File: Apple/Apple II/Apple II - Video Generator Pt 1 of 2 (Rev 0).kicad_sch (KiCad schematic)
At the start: 19 parts

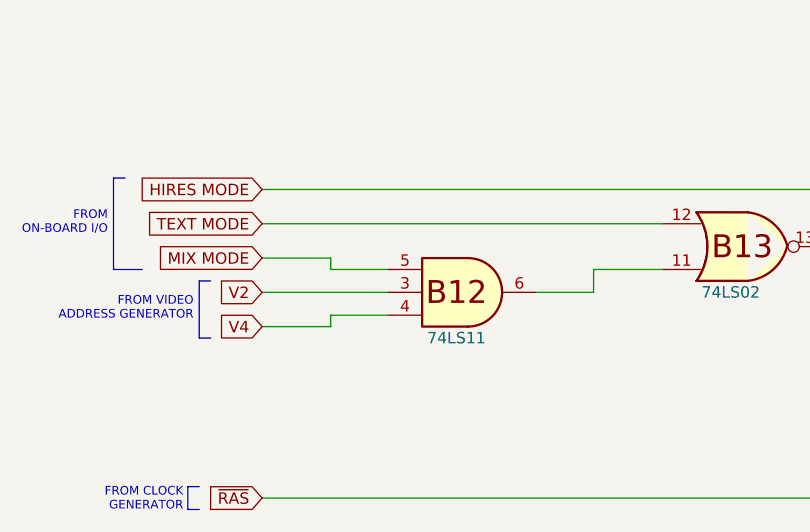
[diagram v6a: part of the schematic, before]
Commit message: Finished Apple II - Single Piece Keyboard
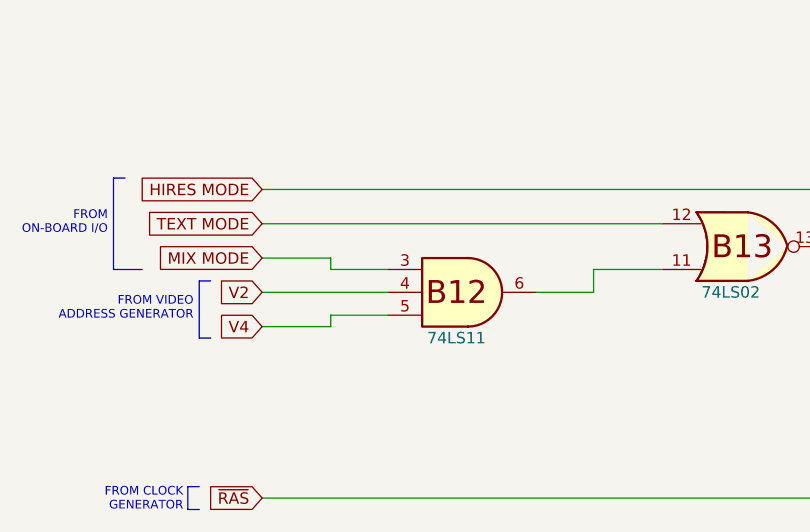
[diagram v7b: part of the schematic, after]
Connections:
- net MIX MODE: now also B12.3; no longer B12.5
- net V2: now also B12.4; no longer B12.3
- net V4: now also B12.5; no longer B12.4
